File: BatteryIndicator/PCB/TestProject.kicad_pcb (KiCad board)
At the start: 2 copper layers, 55.9 x 30.5 mm, 11 parts, among them J1 Conn_01x02_Male, J2 Conn_01x03_Female, J3 Conn_01x07_Female, J3_1 Conn_01x07_Female, J4 Conn_01x02_Male, J5 Conn_01x03_Male, J6 Conn_01x02_Male

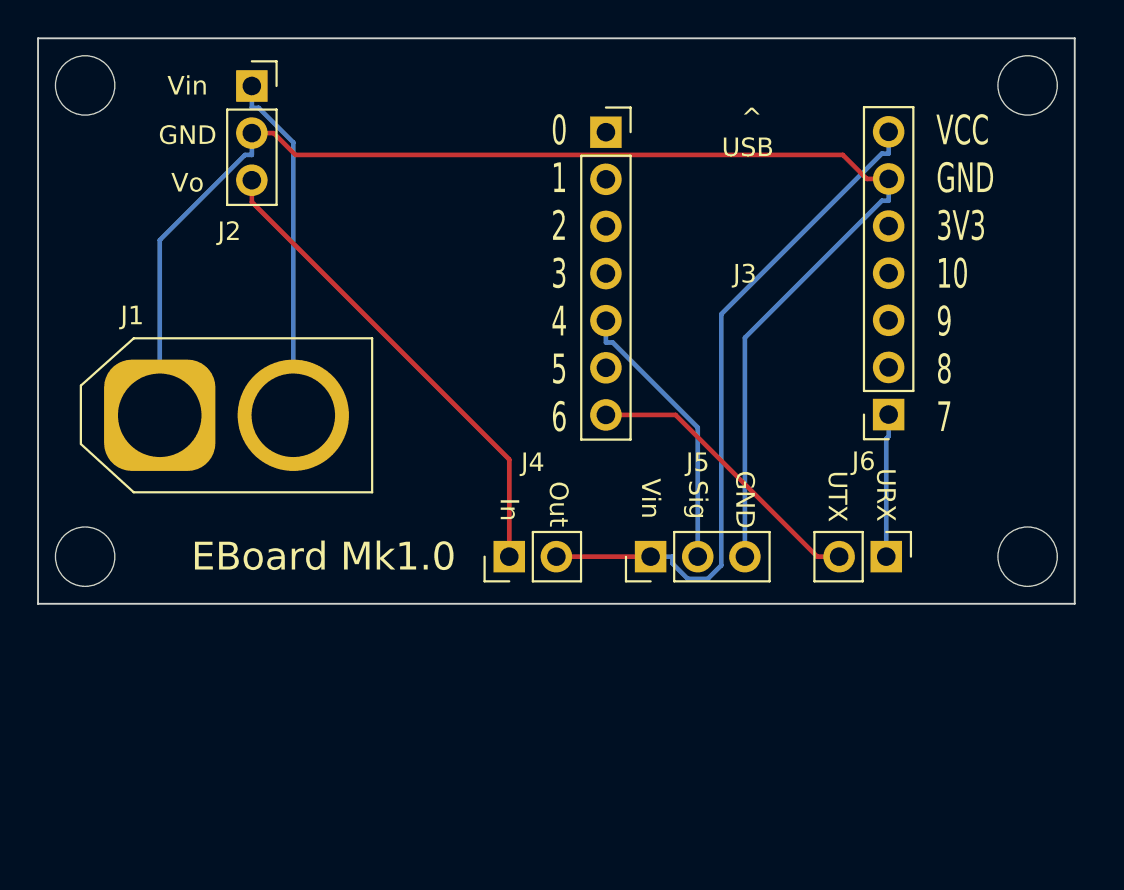
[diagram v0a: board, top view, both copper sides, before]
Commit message: Tried to redo some layout on the PCB
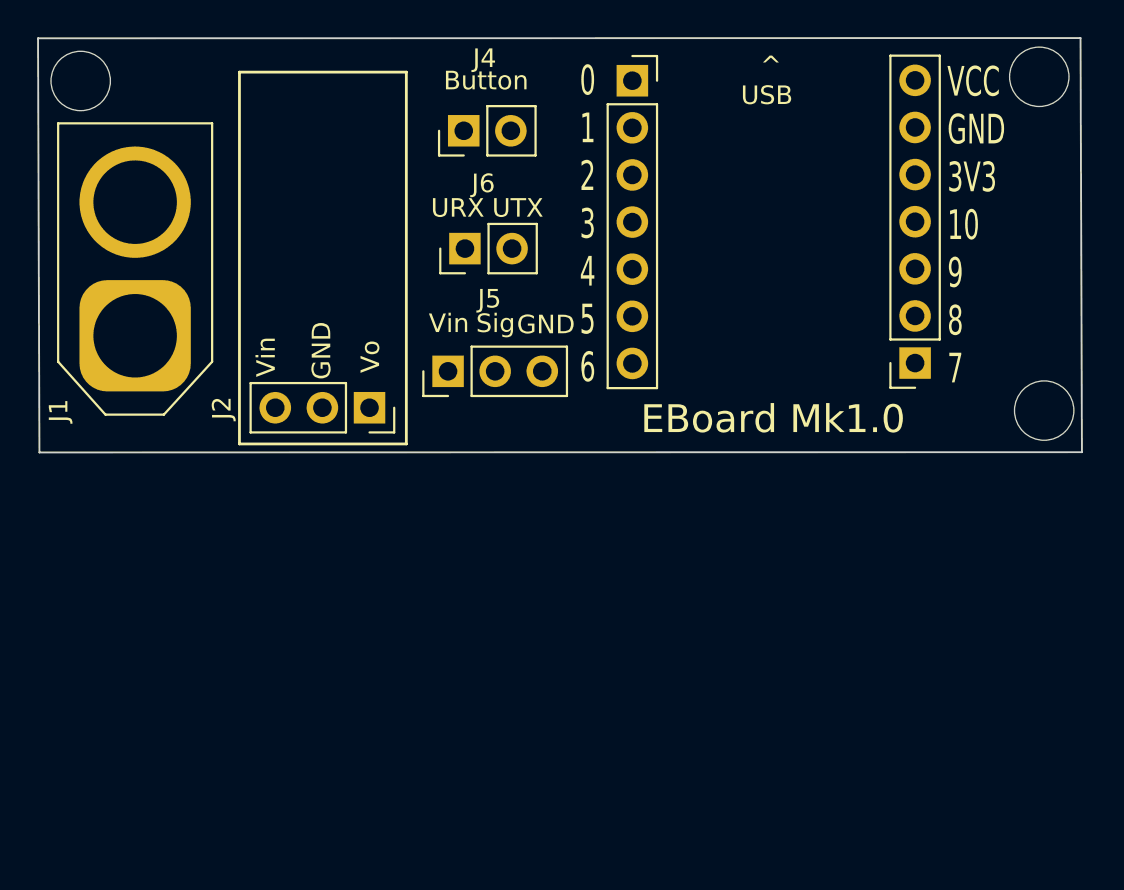
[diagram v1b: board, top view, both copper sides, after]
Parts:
- removed the REF** at (15.2, 40.6)
- moved J6 28.1 mm to (35.7, 24.0), turned to 90 degrees
- moved J4 23.1 mm to (35.6, 17.7)
- moved J2 18.5 mm to (30.6, 32.6), turned to -90 degrees
- moved J5 14.8 mm to (34.8, 30.6)
- moved REF** 7.92 mm to (66.9, 32.8)
- moved J1 4.49 mm to (17.9, 28.7), turned to 90 degrees
- moved J3 3.12 mm to (44.7, 15.0)
- moved J3_1 3.12 mm to (60.0, 30.2)
- moved REF** 0.78 mm to (66.7, 14.8)
- moved REF** 0.34 mm to (15.0, 15.0)
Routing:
- net GND: track 76.6 -> 0.00 mm
- net ButtonOut: track 37.2 -> 0.00 mm
- net V5: track 26.0 -> 0.00 mm
- net Vin: track 18.9 -> 0.00 mm
- net UART TX: track 15.7 -> 0.00 mm
- net SIG_LED: track 15.0 -> 0.00 mm
- net UART RX: track 7.71 -> 0.00 mm
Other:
- board size 55.9 x 30.5 mm -> 56.3 x 22.3 mm
- board text added: "Button"
- board text removed: "In"
- board text removed: "J3"
- board text removed: "Out"

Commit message: edited pcb
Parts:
- J2: moved to B.Cu
- moved J3_1 18.8 mm to (41.2, 31.3)
- moved J3 18.8 mm to (25.9, 16.1)
- moved J2 16.9 mm to (36.3, 16.7), turned to 90 degrees
- moved J5 13.6 mm to (48.3, 32.9), turned to 180 degrees
- moved J4 12.7 mm to (48.3, 17.5), turned to 180 degrees
- moved J6 12.6 mm to (48.3, 23.9), turned to 180 degrees
- moved REF** 11.9 mm to (55.0, 32.8)
- moved REF** 11.7 mm to (55.0, 15.0)
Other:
- board size 56.3 x 22.3 mm -> 44.6 x 22.4 mm
- board text removed: "Vo"

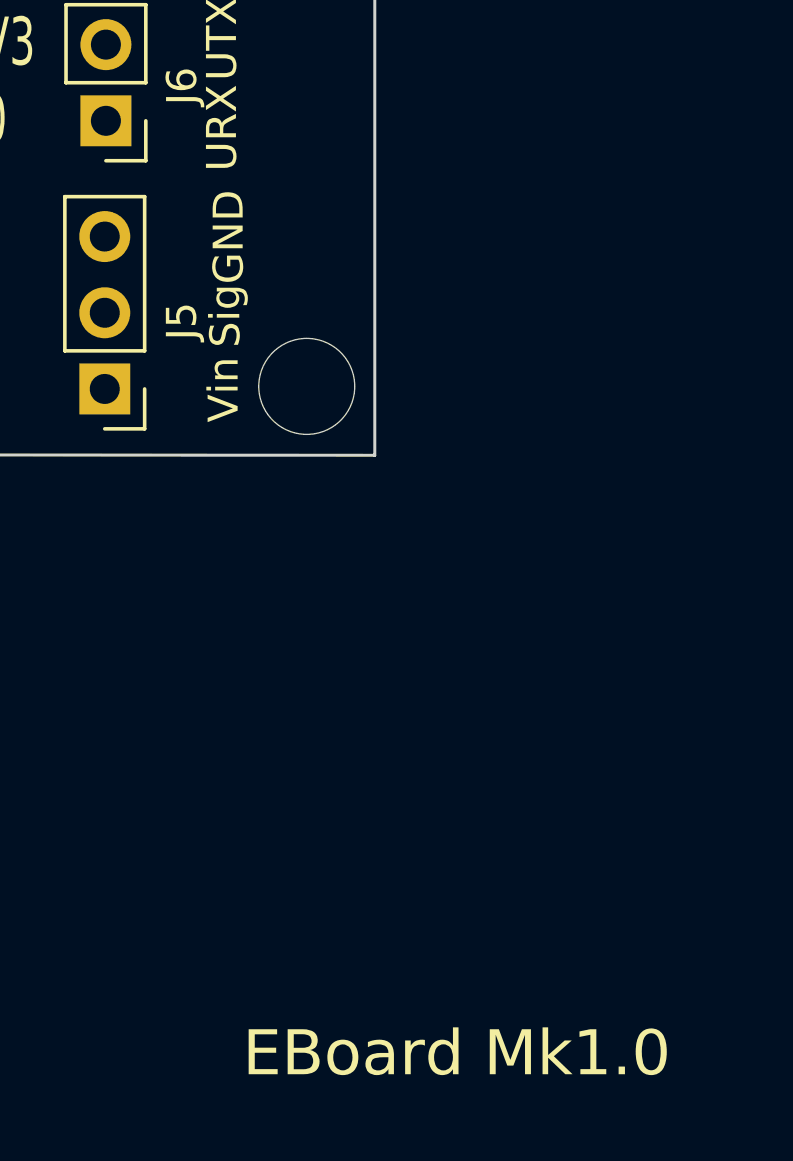
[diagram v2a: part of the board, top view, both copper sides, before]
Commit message: Fixed some markings, changed version to mk1.1
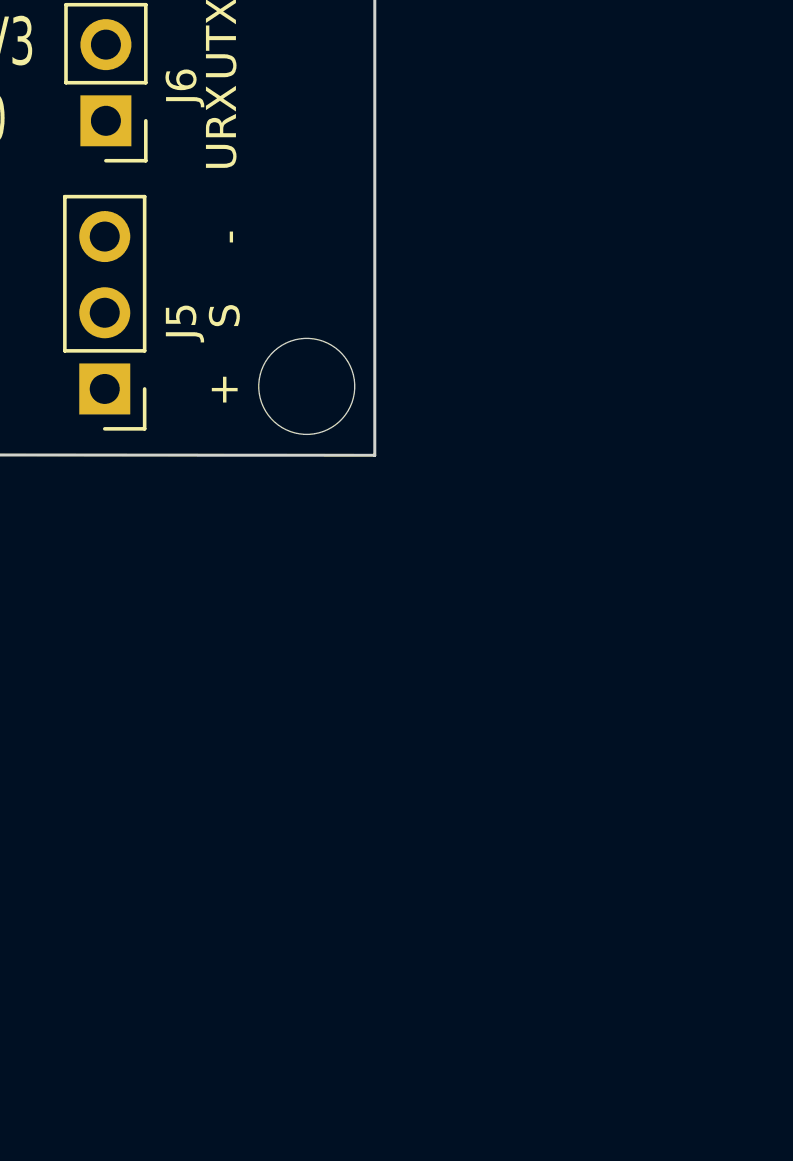
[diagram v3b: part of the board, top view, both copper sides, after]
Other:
- board text added: "+"
- board text added: "-"
- board text added: "EBoard Mk1.1"
- board text added: "J1-Power J2-Buck J3-µC J4-Button J5-LED J6-UART"
- board text added: "S"
- board text removed: "EBoard Mk1.0"
- board text removed: "GND"
- board text removed: "Sig"
- board text removed: "Vin"
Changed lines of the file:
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@@
     (effects (font (size 1 1) (thickness 0.15)) (justify left mirror))
   )
-  (gr_text "GND" (at 52.400854 27.7862 90) (layer "F.SilkS")
+  (gr_text "J1-Power\nJ2-Buck\nJ3-µC\nJ4-Button\nJ5-LED\nJ6-UART" (at 38.1 25.4) (layer "B.SilkS")
+    (effects (font (size 1 1) (thickness 0.15)) (justify left mirror))
+  )
+  (gr_text "EBoard\nMk1.1" (at 53.34 22.86 90) (layer "B.SilkS")
+    (effects (font (size 1.5 1.5) (thickness 0.3)) (justify mirror))
+  )
+  (gr_text "-" (at 52.400854 27.7862 90) (layer "F.SilkS")
     (effects (font (size 1 1) (thickness 0.25)))
   )
@@
     (effects (font (size 1 1) (thickness 0.15)))
   )
-  (gr_text "Sig" (at 52.289037 30.4139 90) (layer "F.SilkS")
+  (gr_text "S" (at 52.289037 30.4139 90) (layer "F.SilkS")
     (effects (font (size 1 1) (thickness 0.25)))
   )
@@
     (effects (font (size 1 1) (thickness 0.25)))
   )
-  (gr_text "EBoard Mk1.0" (at 60 55) (layer "F.SilkS")
-    (effects (font (size 1.5 1.5) (thickness 0.3)))
-  )
-  (gr_text "Vin" (at 52.233129 32.873874 90) (layer "F.SilkS")
+  (gr_text "+" (at 52.233129 32.873874 90) (layer "F.SilkS")
     (effects (font (size 1 1) (thickness 0.25)))
   )
